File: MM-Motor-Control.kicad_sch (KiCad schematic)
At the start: 7 parts, among them J5 Left Header, J6 Right Header, U7 H-Bridge

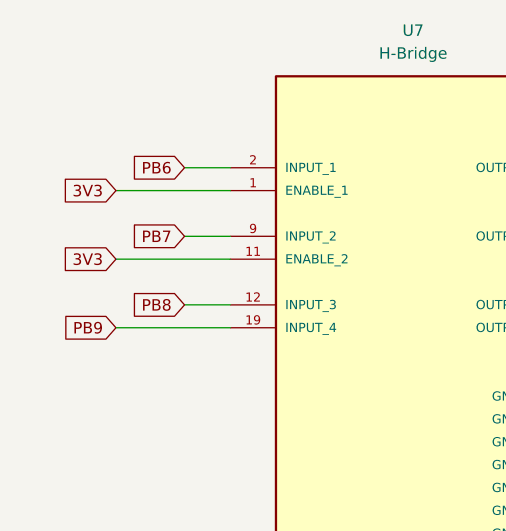
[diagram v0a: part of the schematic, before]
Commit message: added power switch
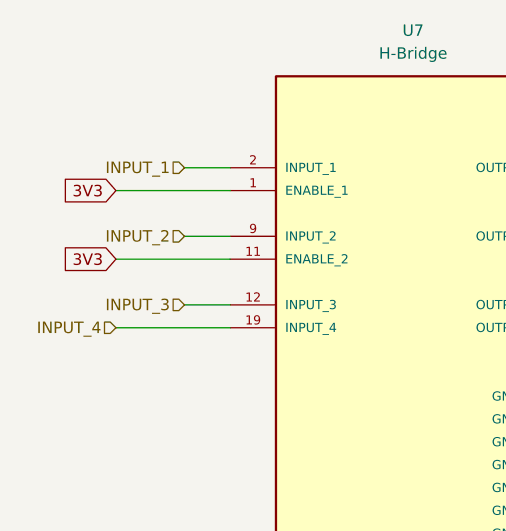
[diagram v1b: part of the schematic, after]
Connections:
- net PB6 renamed INPUT_1
- net PB7 renamed INPUT_2
- net PB8 renamed INPUT_3
- net PB9 renamed INPUT_4

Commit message: fixedled orignetation and linked to ground + duplicated IR emitter/receiver pairs
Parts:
- C34: footprint 0.1µFCapacitor_footprints:CAP_0402_N_WAL-L -> Ceramic_Capacitor_0.1uF_CL21B104KBCNNNC:CAPC2012X95N
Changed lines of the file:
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@@
 			)
 		)
-		(property "Footprint" "0.1µFCapacitor_footprints:CAP_0402_N_WAL-L"
+		(property "Footprint" "Ceramic_Capacitor_0.1uF_CL21B104KBCNNNC:CAPC2012X95N"
 			(at 166.37 78.74 0)
 			(effects

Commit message: Add files via upload
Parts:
- removed C34: 0.1 µF, Ceramic_Capacitor_0.1uF_CL21B104KBCNNNC:CAPC2012X95N, symbol 0.1µFCapacitor_2025-12-15_19-47-12:0402B104K160CT
- added C9: 0.1 µF, CL05A104KA5NNNC:CAPC1005X55N, symbol 0.1µFCapacitor_CL05A104KA5NNNC:CL05A104KA5NNNC
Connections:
- net GND: now also C9.1
- net VCC: now also C9.2

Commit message: redid the 4 emitters receivers, fixed orientation of LEDS and going to continue adding footprints and replace the 60ohm resistors with 300ohm ones
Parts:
- C33: footprint CL21B106KOQNNNE:CAPC2012X140N -> Ceramic_Capacitor_10uF_GRM21BC81C106KA73L:CAPC2012X140N
- C35, C36: footprint CL10A475KP8NNNC:CAPC1608X90N -> Ceramic_Capacitor_4.7uF_CL21A475KAQNNNE:CAPC2012X140N
- C9: footprint CL05A104KA5NNNC:CAPC1005X55N -> Ceramic_Capacitor_0.1uF_CL21B104KBCNNNC:CAPC2012X95N
- U7: footprint hbridge_L293DD:SOIC127P1032X265-20N -> H-Bridge_L293DD:SOIC127P1032X265-20N
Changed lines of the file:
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@@
 			)
 		)
-		(property "Footprint" "CL05A104KA5NNNC:CAPC1005X55N"
+		(property "Footprint" "Ceramic_Capacitor_0.1uF_CL21B104KBCNNNC:CAPC2012X95N"
 			(at 166.37 76.2 0)
 			(effects
@@
 			)
 		)
-		(property "Footprint" "hbridge_L293DD:SOIC127P1032X265-20N"
+		(property "Footprint" "H-Bridge_L293DD:SOIC127P1032X265-20N"
 			(at 125.73 83.82 0)
 			(effects
@@
 			)
 		)
-		(property "Footprint" "CL10A475KP8NNNC:CAPC1608X90N"
+		(property "Footprint" "Ceramic_Capacitor_4.7uF_CL21A475KAQNNNE:CAPC2012X140N"
 			(at 189.23 73.66 0)
 			(effects
@@
 			)
 		)
-		(property "Footprint" "CL10A475KP8NNNC:CAPC1608X90N"
+		(property "Footprint" "Ceramic_Capacitor_4.7uF_CL21A475KAQNNNE:CAPC2012X140N"
 			(at 189.23 63.5 0)
 			(effects
@@
 			)
 		)
-		(property "Footprint" "CL21B106KOQNNNE:CAPC2012X140N"
+		(property "Footprint" "Ceramic_Capacitor_10uF_GRM21BC81C106KA73L:CAPC2012X140N"
 			(at 166.37 66.04 0)
 			(effects

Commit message: PCB tentative finished
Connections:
- net INPUT_3: now also U7.19 (INPUT_4); no longer U7.12 (INPUT_3)
- net INPUT_4: now also U7.12 (INPUT_3); no longer U7.19 (INPUT_4)
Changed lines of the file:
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@@
 		)
 	)
-	(hierarchical_label "INPUT_4"
+	(hierarchical_label "INPUT_3"
 		(shape input)
 		(at 92.71 93.98 180)
@@
 		)
 	)
-	(hierarchical_label "INPUT_3"
+	(hierarchical_label "INPUT_4"
 		(shape input)
 		(at 100.33 91.44 180)

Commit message: finished edits on PCB - hopefully final
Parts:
- removed J5: Left Header, Connector_PinHeader_1.27mm:PinHeader_1x06_P1.27mm_Vertical_SMD_Pin1Left, symbol Connector:Conn_01x06_Pin
- removed J6: Right Header, Connector_PinHeader_1.27mm:PinHeader_1x06_P1.27mm_Vertical_SMD_Pin1Right, symbol Connector:Conn_01x06_Pin
- added J2, J3: Conn_01x06, Connector_PinHeader_2.54mm:PinHeader_1x06_P2.54mm_Vertical, symbol Connector_Generic:Conn_01x06
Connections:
- net 3V3: now also J2.3 (Pin_3), J3.3 (Pin_3)
- net GND: now also J2.6 (Pin_6), J3.6 (Pin_6)
- net LENC1: now also J2.5 (Pin_5)
- net LENC2: now also J2.4 (Pin_4)
- net ML1: now also J2.1 (Pin_1)
- net ML2: now also J2.2 (Pin_2)
- net MR1: now also J3.1 (Pin_1)
- net MR2: now also J3.2 (Pin_2)
- net RENC1: now also J3.5 (Pin_5)
- net RENC2: now also J3.4 (Pin_4)
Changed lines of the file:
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@@
 	)
 	(symbol
-		(lib_id "Connector:Conn_01x06_Pin")
-		(at 132.08 134.62 0)
+		(lib_id "Connector_Generic:Conn_01x06")
+		(at 132.08 137.16 180)
 		(unit 1)
 		(exclude_from_sim no)
@@
 		(dnp no)
 		(fields_autoplaced yes)
-		(property "Reference" "J6"
-			(at 132.715 124.46 0)
-			(effects
-				(font
-					(size 1.27 1.27)
-				)
-			)
-		)
-		(property "Value" "Right Header"
-			(at 132.715 127 0)
-			(effects
-				(font
-					(size 1.27 1.27)
-				)
-			)
-		)
-		(property "Footprint" "Connector_PinHeader_1.27mm:PinHeader_1x06_P1.27mm_Vertical_SMD_Pin1Right"
-			(at 132.08 134.62 0)
+		(property "Reference" "J3"
+			(at 132.08 123.19 0)
+			(effects
+				(font
+					(size 1.27 1.27)
+				)
+			)
+		)
+		(property "Value" "Conn_01x06"
+			(at 132.08 125.73 0)
+			(effects
+				(font
+					(size 1.27 1.27)
+				)
+			)
+		)
+		(property "Footprint" "Connector_PinHeader_2.54mm:PinHeader_1x06_P2.54mm_Vertical"
+			(at 132.08 137.16 0)
 			(effects
 				(font
@@
 		)
 		(property "Datasheet" "~"
-			(at 132.08 134.62 0)
-			(effects
-				(font
-					(size 1.27 1.27)
-				)
-				(hide yes)
-			)
-		)
-		(property "Description" "Generic connector, single row, 01x06, script generated"
-			(at 132.08 134.62 0)
-			(effects
-				(font
-					(size 1.27 1.27)
-				)
-				(hide yes)
-			)
+			(at 132.08 137.16 0)
+			(effects
+				(font
+					(size 1.27 1.27)
+				)
+				(hide yes)
+			)
+		)
+		(property "Description" "Generic connector, single row, 01x06, script generated (kicad-library-utils/schlib/autogen/connector/)"
+			(at 132.08 137.16 0)
+			(effects
+				(font
+					(size 1.27 1.27)
+				)
+				(hide yes)
+			)
+		)
+		(pin "4"
+		)
+		(pin "5"
+		)
+		(pin "1"
 		)
 		(pin "3"
@@
 		)
 		(pin "6"
-		)
-		(pin "1"
-		)
-		(pin "5"
-		)
-		(pin "4"
 		)
 		(instances
 			(project "IREmitter"
 				(path "/d311851a-8b0b-4acf-b2e7-1b968b2adbe7/1d0e5a43-54ed-4736-85fc-b571bbabafee"
-					(reference "J6")
+					(reference "J3")
+					(unit 1)
+				)
+			)
+		)
+	)
+	(symbol
+		(lib_id "Connector_Generic:Conn_01x06")
+		(at 119.38 134.62 0)
+		(unit 1)
+		(exclude_from_sim no)
+		(in_bom yes)
+		(on_board yes)
+		(dnp no)
+		(property "Reference" "J2"
+			(at 115.57 144.78 0)
+			(effects
+				(font
+					(size 1.27 1.27)
+				)
+				(justify left)
+			)
+		)
+		(property "Value" "Conn_01x06"
+			(at 115.57 147.32 0)
+			(effects
+				(font
+					(size 1.27 1.27)
+				)
+				(justify left)
+			)
+		)
+		(property "Footprint" "Connector_PinHeader_2.54mm:PinHeader_1x06_P2.54mm_Vertical"
+			(at 119.38 134.62 0)
+			(effects
+				(font
+					(size 1.27 1.27)
+				)
+				(hide yes)
+			)
+		)
+		(property "Datasheet" "~"
+			(at 119.38 134.62 0)
+			(effects
+				(font
+					(size 1.27 1.27)
+				)
+				(hide yes)
+			)
+		)
+		(property "Description" "Generic connector, single row, 01x06, script generated (kicad-library-utils/schlib/autogen/connector/)"
+			(at 119.38 134.62 0)
+			(effects
+				(font
+					(size 1.27 1.27)
+				)
+				(hide yes)
+			)
+		)
+		(pin "4"
+		)
+		(pin "5"
+		)
+		(pin "1"
+		)
+		(pin "3"
+		)
+		(pin "2"
+		)
+		(pin "6"
+		)
+		(instances
+			(project ""
+				(path "/d311851a-8b0b-4acf-b2e7-1b968b2adbe7/1d0e5a43-54ed-4736-85fc-b571bbabafee"
+					(reference "J2")
 					(unit 1)
 				)
@@
 					(unit 1)
 				)
-			)
-		)
-	)
-	(symbol
-		(lib_id "Connector:Conn_01x06_Pin")
-		(at 119.38 137.16 180)
-		(unit 1)
-		(exclude_from_sim no)
-		(in_bom yes)
-		(on_board yes)
-		(dnp no)
-		(property "Reference" "J5"
-			(at 115.316 124.46 0)
-			(effects
-				(font
-					(size 1.27 1.27)
-				)
-				(justify right)
-			)
-		)
-		(property "Value" "Left Header"
-			(at 111.76 127 0)
-			(effects
-				(font
-					(size 1.27 1.27)
-				)
-				(justify right)
-			)
-		)
-		(property "Footprint" "Connector_PinHeader_1.27mm:PinHeader_1x06_P1.27mm_Vertical_SMD_Pin1Left"
-			(at 119.38 137.16 0)
-			(effects
-				(font
-					(size 1.27 1.27)
-				)
-				(hide yes)
-			)
-		)
-		(property "Datasheet" "~"
-			(at 119.38 137.16 0)
-			(effects
-				(font
-					(size 1.27 1.27)
-				)
-				(hide yes)
-			)
-		)
-		(property "Description" "Generic connector, single row, 01x06, script generated"
-			(at 119.38 137.16 0)
-			(effects
-				(font
-					(size 1.27 1.27)
-				)
-				(hide yes)
-			)
-		)
-		(pin "1"
-		)
-		(pin "2"
-		)
-		(pin "3"
-		)
-		(pin "4"
-		)
-		(pin "5"
-		)
-		(pin "6"
-		)
-		(instances
-			(project "IREmitter"
-				(path "/d311851a-8b0b-4acf-b2e7-1b968b2adbe7/1d0e5a43-54ed-4736-85fc-b571bbabafee"
-					(reference "J5")
-					(unit 1)
-				)
